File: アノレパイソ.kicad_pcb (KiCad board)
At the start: 2 copper layers, 27 parts, among them SW1 RotaryEncoder_Switch, SW2 SW_PUSH, SW3 SW_PUSH, SW5 SW_PUSH, SW6 SW_PUSH, SW7 SW_PUSH, SW8 SW_PUSH, SW9 SW_PUSH

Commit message: PCBエディタで可能な限り部品の配置と配線を実施
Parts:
- added U2: SO1602AWWB-UC-WB-U, AKI-SO1602AWGB:SO1602AWWB-UC-WB-U, F.Cu at (184.5, 75.0)
- moved LED11 130.0 mm to (125.1, 84.8), turned to -90 degrees
- moved LED12 126.0 mm to (145.0, 85.0), turned to -90 degrees
- moved LED10 120.8 mm to (117.5, 91.5), turned to -90 degrees
- moved LED7 120.7 mm to (65.6, 89.8), turned to -90 degrees
- moved LED8 118.3 mm to (86.5, 89.8), turned to -90 degrees
- moved LED9 113.9 mm to (107.5, 89.7), turned to -90 degrees
- moved LED6 102.7 mm to (65.5, 68.8), turned to 90 degrees
- moved SW1 80.8 mm to (137.5, 67.5), turned to -90 degrees
- moved SW7 79.2 mm to (85.1, 80.4)
- moved SW9 79.1 mm to (106.1, 80.4)
- moved SW5 79.1 mm to (64.1, 80.4)
- moved SW8 76.6 mm to (106.1, 59.5)
- moved SW6 75.8 mm to (85.0, 59.5)
- moved SW2 75.6 mm to (64.0, 59.5)
- moved LED5 64.0 mm to (86.6, 68.8), turned to 90 degrees
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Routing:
- net Net-(LED6-DOUT): track 0.00 -> 33.4 mm
- net Net-(LED5-DOUT): track 0.00 -> 20.8 mm
- net Net-(LED4-DOUT): track 0.00 -> 20.7 mm
- net Net-(LED8-DOUT): track 0.00 -> 20.7 mm
- net Net-(LED7-DOUT): track 0.00 -> 20.6 mm
- net Net-(LED11-DOUT): track 0.00 -> 19.7 mm
- net Net-(LED1-DOUT): track 0.00 -> 19.0 mm
- net Net-(LED2-DOUT): track 0.00 -> 12.4 mm
- net Net-(LED3-DOUT): track 0.00 -> 10.9 mm
- net Net-(LED10-DIN): track 0.00 -> 10.4 mm
- net Net-(LED10-DOUT): track 0.00 -> 7.22 mm
- net Net-(D3-A): track 0.00 -> 6.09 mm
- net Net-(D2-A): track 0.00 -> 6.09 mm
- net Net-(D1-A): track 0.00 -> 6.02 mm
- net Net-(D6-A): track 0.00 -> 5.60 mm
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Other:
- board outline added: 170 x 50 mm

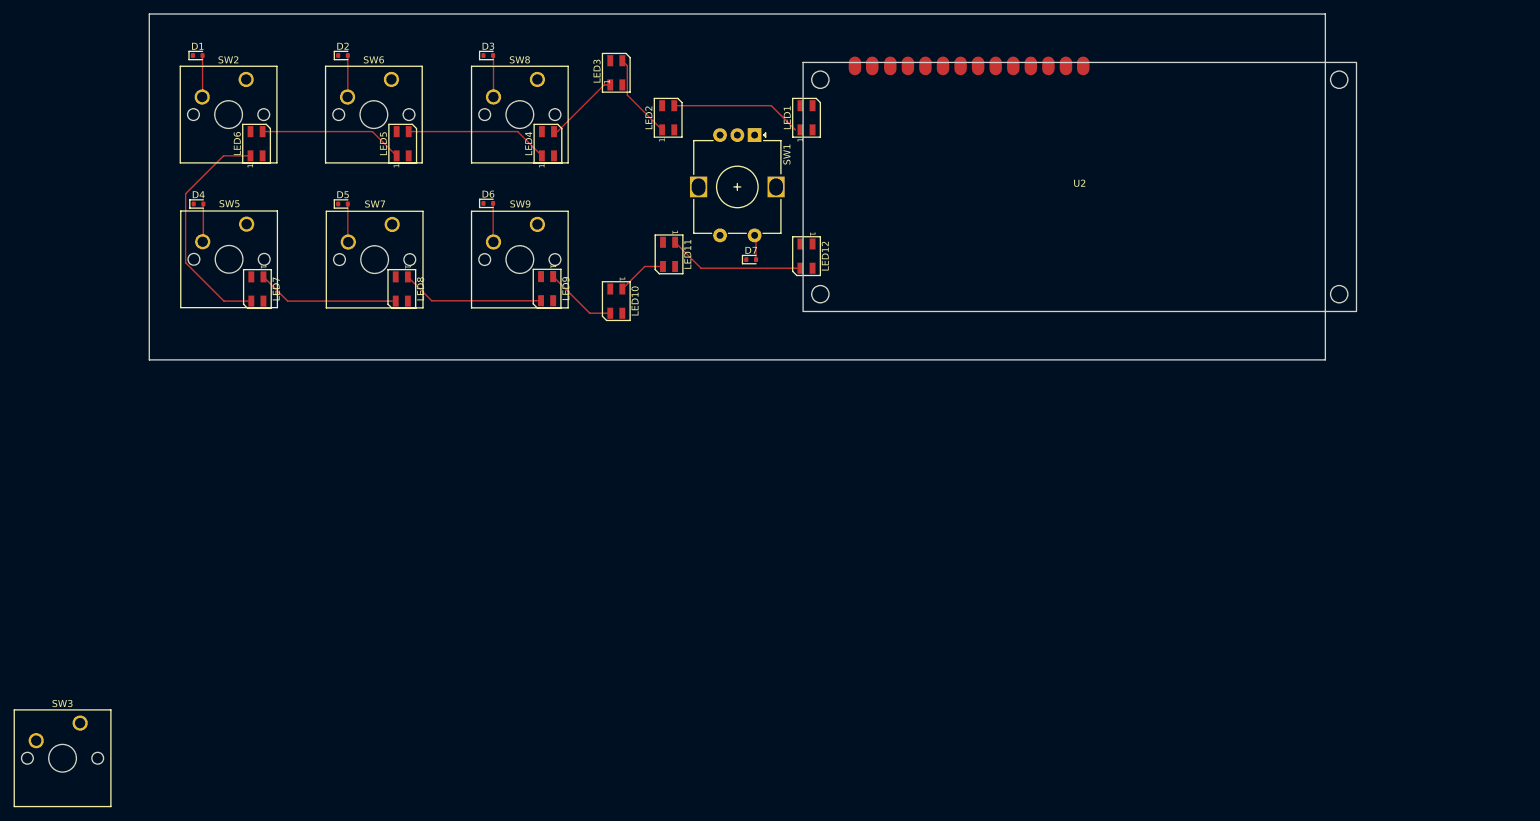
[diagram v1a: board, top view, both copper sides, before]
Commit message: μCOMを残して配線完了。
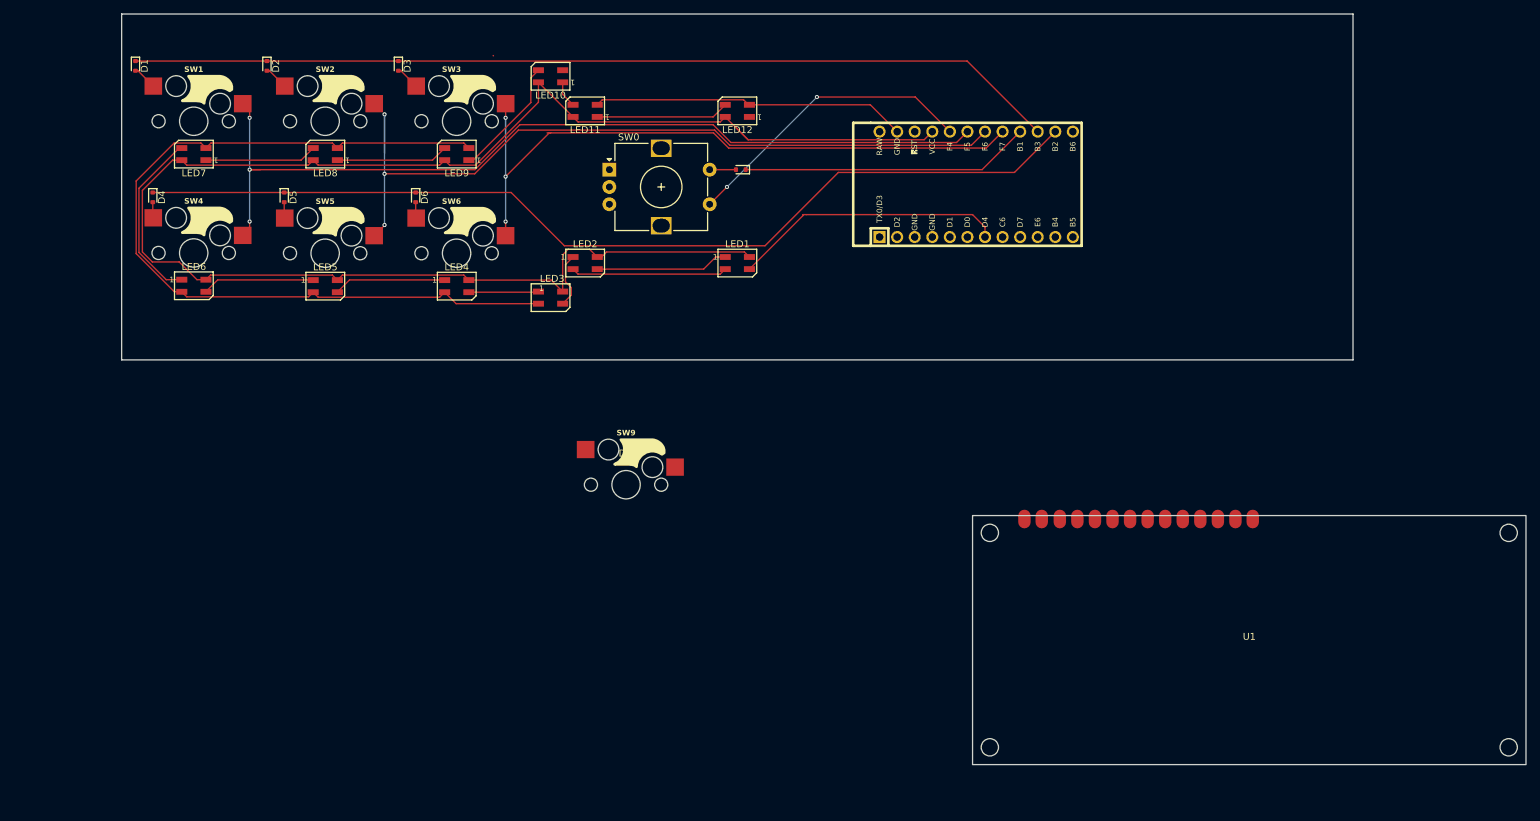
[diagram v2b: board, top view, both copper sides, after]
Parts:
- removed D7: 1N4148WT, Diode_SMD:D_SOD-523
- removed SW7, SW8: SW_PUSH, Button_Switch_Keyboard:SW_Cherry_MX_1.00u_PCB
- removed U2: SO1602AWWB-UC-WB-U, AKI-SO1602AWGB:SO1602AWWB-UC-WB-U
- added D0: 1N4148WT, Diode_SMD:D_SOD-523, F.Cu at (135.5, 72.5)
- added SW0: RotaryEncoder_Switch, Rotary_Encoder:RotaryEncoder_Alps_EC12E-Switch_Vertical_H20mm, F.Cu at (116.5, 72.5)
- added SW4: SW_PUSH, kbd-main:keyswitch_cherrymx_hotswap_1u, F.Cu at (56.4, 84.5)
- added U1: SO1602AWWB-UC-WB-U, AKI-SO1602AWGB:SO1602AWWB-UC-WB-U, F.Cu at (209.0, 140.5)
- added U3: ProMicro, Keebio-Parts.pretty-master:ArduinoProMicro, F.Cu at (169.5, 74.6)
- SW1: value RotaryEncoder_Switch -> SW_PUSH; footprint Rotary_Encoder:RotaryEncoder_Alps_EC12E-Switch_Vertical_H20mm -> kbd-main:keyswitch_cherrymx_hotswap_1u
- SW2, SW3, SW5, SW6, SW9: footprint Button_Switch_Keyboard:SW_Cherry_MX_1.00u_PCB -> kbd-main:keyswitch_cherrymx_hotswap_1u
- moved SW3 102.6 mm to (94.4, 65.5)
- moved SW1 81.1 mm to (56.4, 65.5), turned to 0 degrees
- moved SW9 39.7 mm to (118.9, 118.0)
- moved LED10 33.9 mm to (108.0, 59.0), turned to 180 degrees
- moved LED3 33.9 mm to (108.0, 91.0), turned to 0 degrees
- moved SW6 26.8 mm to (94.4, 84.6)
- moved LED4 24.4 mm to (94.4, 89.3), turned to 0 degrees
- moved LED2 24.2 mm to (113.0, 86.0), turned to 0 degrees
- moved LED11 24.0 mm to (113.0, 64.0), turned to 180 degrees
- moved LED9 23.4 mm to (94.4, 70.2), turned to 180 degrees
- moved LED5 23.4 mm to (75.4, 89.3), turned to 0 degrees
- moved LED1 23.3 mm to (135.0, 86.0), turned to 0 degrees
- moved LED12 23.3 mm to (135.0, 64.0), turned to 180 degrees
- moved LED6 22.4 mm to (56.4, 89.3), turned to 0 degrees
- moved LED8 22.4 mm to (75.4, 70.2), turned to 180 degrees
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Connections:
- SW2 pad 1: Col1 -> Col2
- SW2 pad 2: Net-(D1-A) -> Net-(D2-A)
- SW3 pad 1: Reset -> Col3
- SW3 pad 2: GND -> Net-(D3-A)
- SW5 pad 1: Col1 -> Col2
- SW5 pad 2: Net-(D4-A) -> Net-(D5-A)
- SW6 pad 1: Col2 -> Col3
- SW6 pad 2: Net-(D2-A) -> Net-(D6-A)
- SW9 pad 1: Col3 -> Reset
- SW9 pad 2: Net-(D6-A) -> GND
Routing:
- net VCC: track 0.00 -> 237.9 mm
- net GND: track 0.00 -> 192.8 mm
- net Row2: track 0.00 -> 140.5 mm
- net Row1: track 0.00 -> 134.6 mm
- net Col1: track 0.00 -> 129.6 mm, vias 0 -> 3
- net Col2: track 0.00 -> 114.9 mm, vias 0 -> 3
- net Col3: track 0.00 -> 98.4 mm, vias 0 -> 3
- net Col0: track 0.00 -> 43.2 mm, vias 0 -> 2
- net Row0: track 0.00 -> 42.0 mm
- net LED: track 0.00 -> 39.6 mm
- net Net-(LED6-DOUT): track 33.4 -> 25.7 mm
- net Net-(LED10-DIN): track 10.4 -> 17.5 mm
- net Net-(LED5-DOUT): track 20.8 -> 16.2 mm
- net Net-(LED4-DOUT): track 20.7 -> 16.2 mm
- net Net-(LED8-DOUT): track 20.7 -> 16.2 mm
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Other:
- board size 170 x 50 mm -> 178 x 50 mm

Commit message: いったん今の知識でやれることは全部終わり。赤ペン待ち。
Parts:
- SW9: footprint kbd-main:keyswitch_cherrymx_hotswap_1u -> kbd-main:ResetSW
- moved SW9 91.3 mm to (183.5, 53.5)
- moved U1 14.1 mm to (223.0, 142.0)
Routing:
- net GND: track 192.8 -> 345.9 mm, vias 0 -> 2
- net RE_B: track 0.00 -> 74.1 mm
- net RE_A: track 0.00 -> 73.3 mm
- net Reset: track 0.00 -> 35.3 mm
- net SCL: track 0.00 -> 24.4 mm, vias 0 -> 1
- net VCC: track 237.9 -> 259.6 mm, vias 0 -> 1
- net Net-(LED10-DIN): track 17.5 -> 18.7 mm
- net Col0: track 43.2 -> 43.9 mm
- net unconnected-(U1-SDAout-Pad9): vias 0 -> 1
- net unconnected-(U1-SAO-Pad4): vias 0 -> 1
- net unconnected-(U1-NC-Pad6): vias 0 -> 1
- net unconnected-(U1-NC-Pad5): vias 0 -> 1
- net unconnected-(U1-NC-Pad14): vias 0 -> 1
- net unconnected-(U1-NC-Pad13): vias 0 -> 1
- net unconnected-(U1-NC-Pad12): vias 0 -> 1
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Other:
- board text added: "/CS"
- board text added: "LHD-335J"
- board text added: "NC"
- board text added: "RHD-335J"
- board text added: "SA0"
- board text added: "SCL"
- board text added: "SDA_in"
- board text added: "SDA_out"
- board text added: "VDD"
- board text added: "VSS"
- board text added: "ﾉﾉﾉﾉﾉアﾉﾚパイソ"

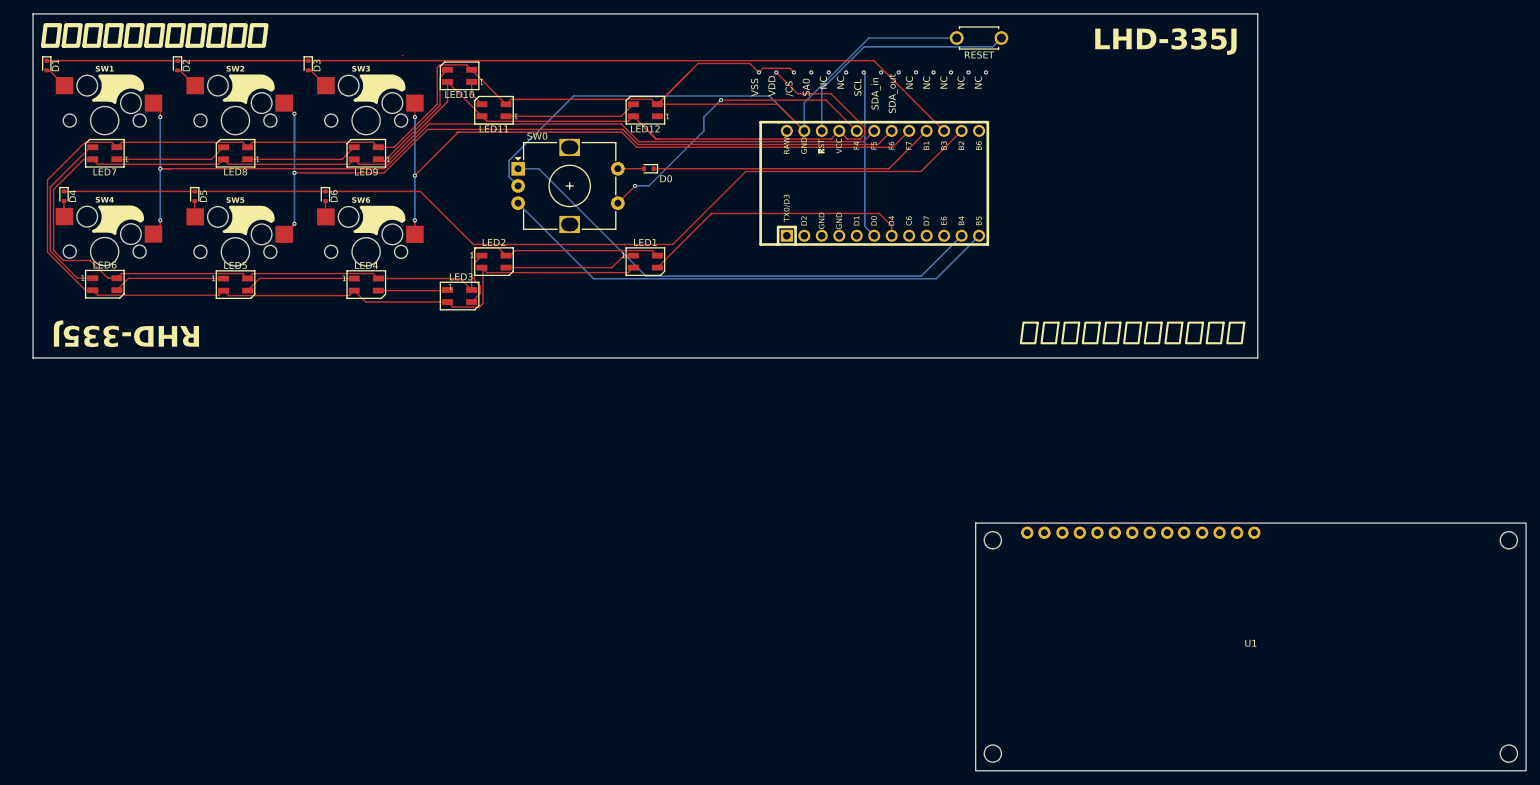
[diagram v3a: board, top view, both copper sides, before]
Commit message: 電気系のエラーはすべてなくした。
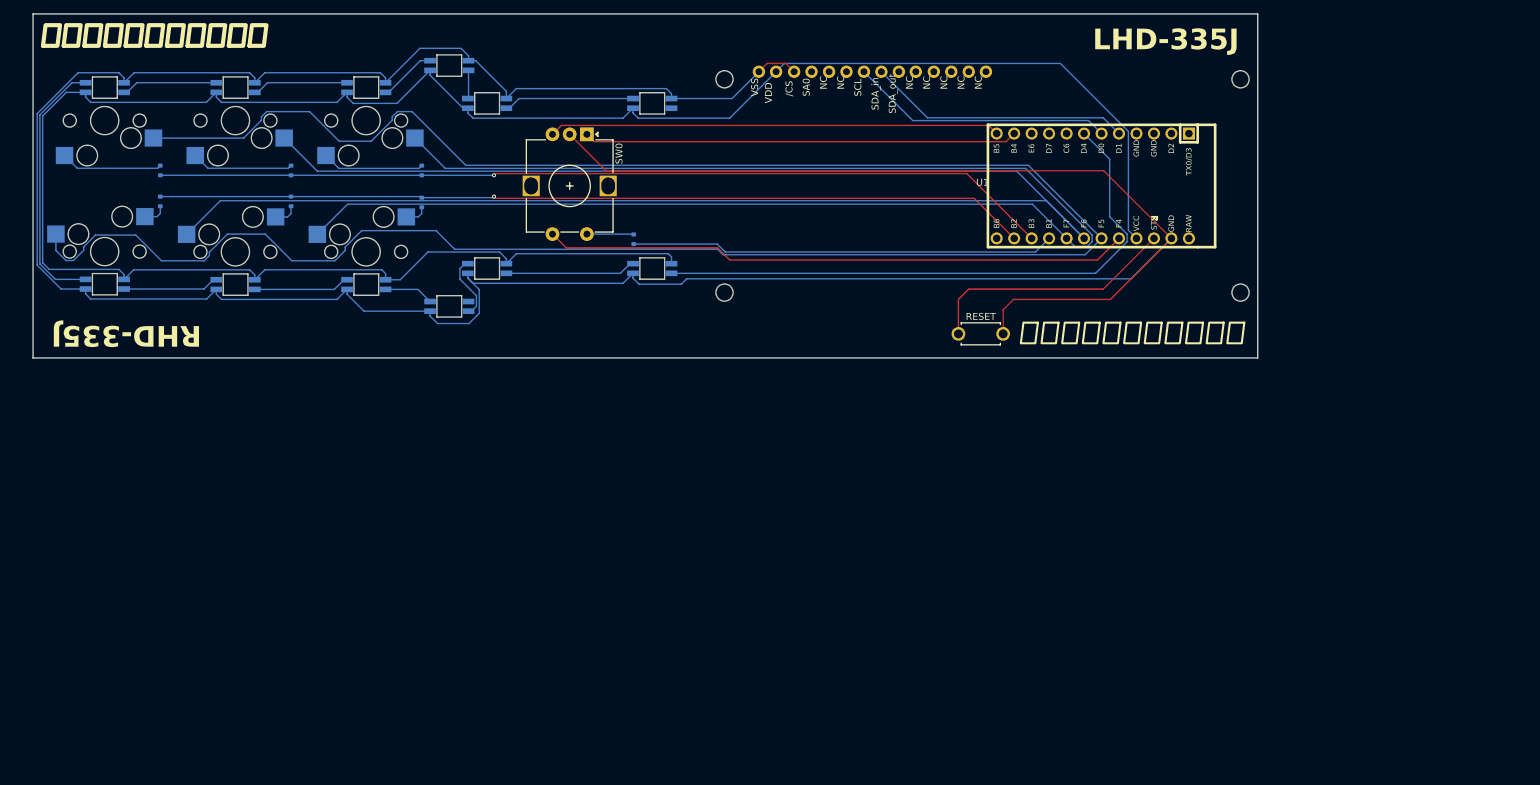
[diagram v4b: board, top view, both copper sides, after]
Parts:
- D0, D1, D2, D3, D4, D5, D6, SW1, SW2, SW3, SW4, SW5, SW6: moved to B.Cu
- LED1, LED10, LED11, LED12, LED2, LED3, LED4, LED5, LED6, LED7, LED8, LED9: footprint LED_SMD:LED_SK6812MINI_PLCC4_3.5x3.5mm_P1.75mm -> kbd-main:YS-SK6812MINI-E; moved to B.Cu
- moved U1 77.5 mm to (184.0, 75.0)
- moved SW9 43.0 mm to (183.8, 96.5), turned to 180 degrees
- moved U3 30.5 mm to (200.0, 75.0), turned to 180 degrees
- moved D1 22.5 mm to (64.5, 72.8), turned to 90 degrees
- moved D2 22.5 mm to (83.5, 72.8), turned to 90 degrees
- moved D3 22.5 mm to (102.5, 72.8), turned to 90 degrees
- moved D6 14.0 mm to (102.5, 77.4)
- moved D4 14.0 mm to (64.5, 77.2)
- moved D5 14.0 mm to (83.5, 77.2)
- moved SW0 11.2 mm to (126.5, 67.5), turned to -90 degrees
- moved D0 10.5 mm to (133.3, 82.8), turned to 90 degrees
- moved LED7 9.55 mm to (56.4, 60.7), turned to 0 degrees
- moved LED8 9.55 mm to (75.4, 60.7), turned to 0 degrees
- moved LED9 9.55 mm to (94.4, 60.7), turned to 0 degrees
- moved LED10 2.12 mm to (106.5, 57.5), turned to 0 degrees
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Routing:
- net Col1: track 129.6 -> 317.5 mm, vias 3 -> 0
- net Col2: track 114.9 -> 257.0 mm, vias 3 -> 0
- net Col3: track 98.4 -> 222.5 mm, vias 3 -> 0
- net GND: track 345.9 -> 460.9 mm, vias 2 -> 0
- net VCC: track 259.6 -> 316.3 mm, vias 1 -> 0
- net LED: track 39.6 -> 86.4 mm
- net Col0: track 43.9 -> 85.2 mm, vias 2 -> 0
- net SDA: track 0.00 -> 38.3 mm
- net Row0: track 42.0 -> 61.7 mm
- net SCL: track 24.4 -> 38.3 mm, vias 1 -> 0
- net Row2: track 140.5 -> 126.7 mm, vias 0 -> 1
- net Net-(D3-A): track 3.57 -> 16.0 mm
- net Net-(LED6-DOUT): track 25.7 -> 37.8 mm
- net Net-(D1-A): track 3.50 -> 14.8 mm
- net Net-(D2-A): track 3.50 -> 14.8 mm
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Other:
- board text added: "Perfecting Art of Electrowireing"
